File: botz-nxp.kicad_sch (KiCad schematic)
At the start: 12 parts, among them IC1 MCXA265VLH, J1 microSD, J2 JST_1mm_4, U2 MCP2561-E-MF, U3 MCP2561-E-MF

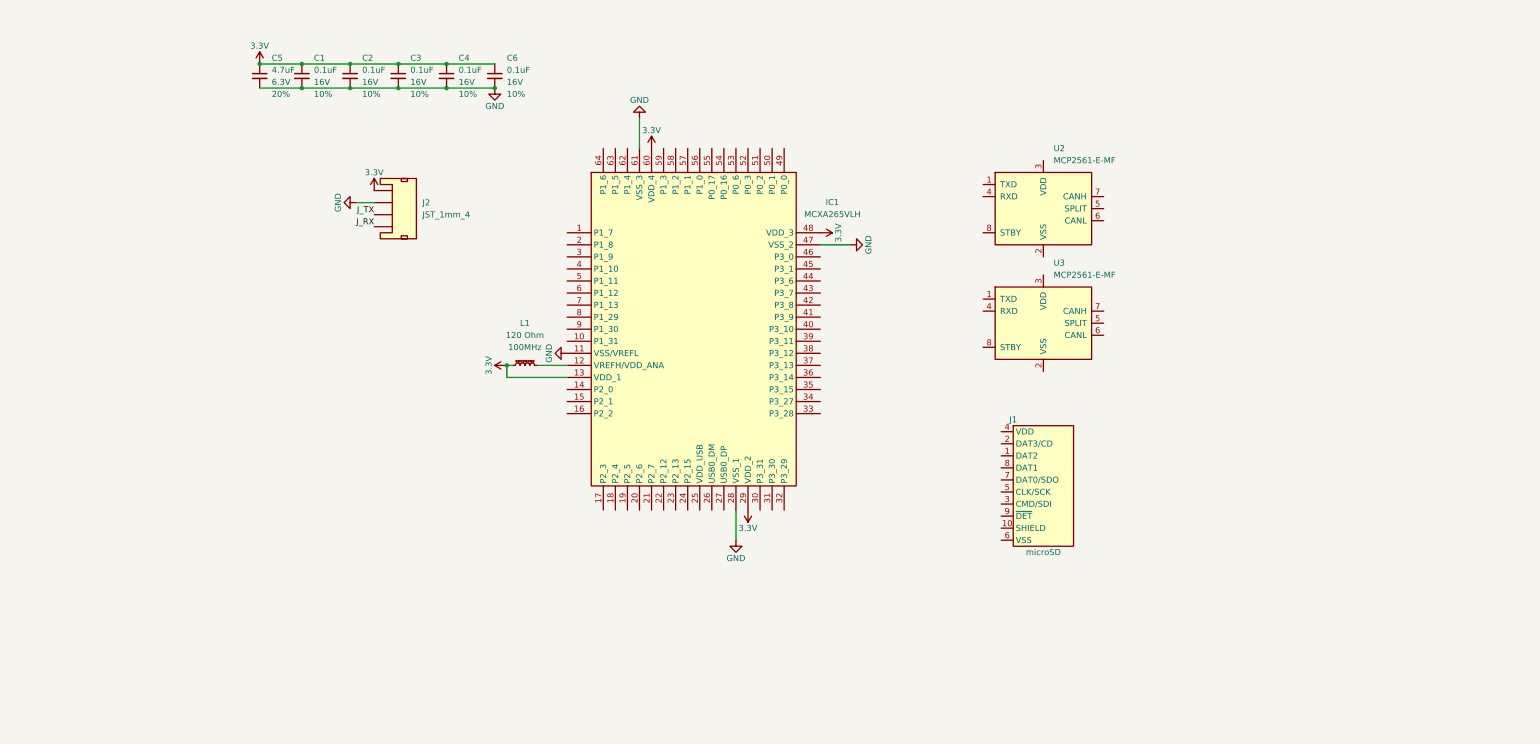
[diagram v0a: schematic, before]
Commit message: Wire CAN0/CAN1, microSD (SPI), reset, crystal, SWD header
- CAN0 on P1_2/P1_3, CAN1 on P1_1/P1_0 (ALT11), MCP2561 transceivers
- 120R termination, jumper-selectable (JP1/JP2)
- microSD on LPSPI1 (P3_8-P3_11), pull-ups, card detect on P2_2
- NRST pull-up + filter cap, crystal on P1_30/P1_31 (15pF placeholder)
- 10-pin Cortex SWD header on P0_0-P0_2
- Bulk cap swapped to 10uF 25V; VDDA filter caps after L1
- Commit lib/ and library tables so the project opens on other machines
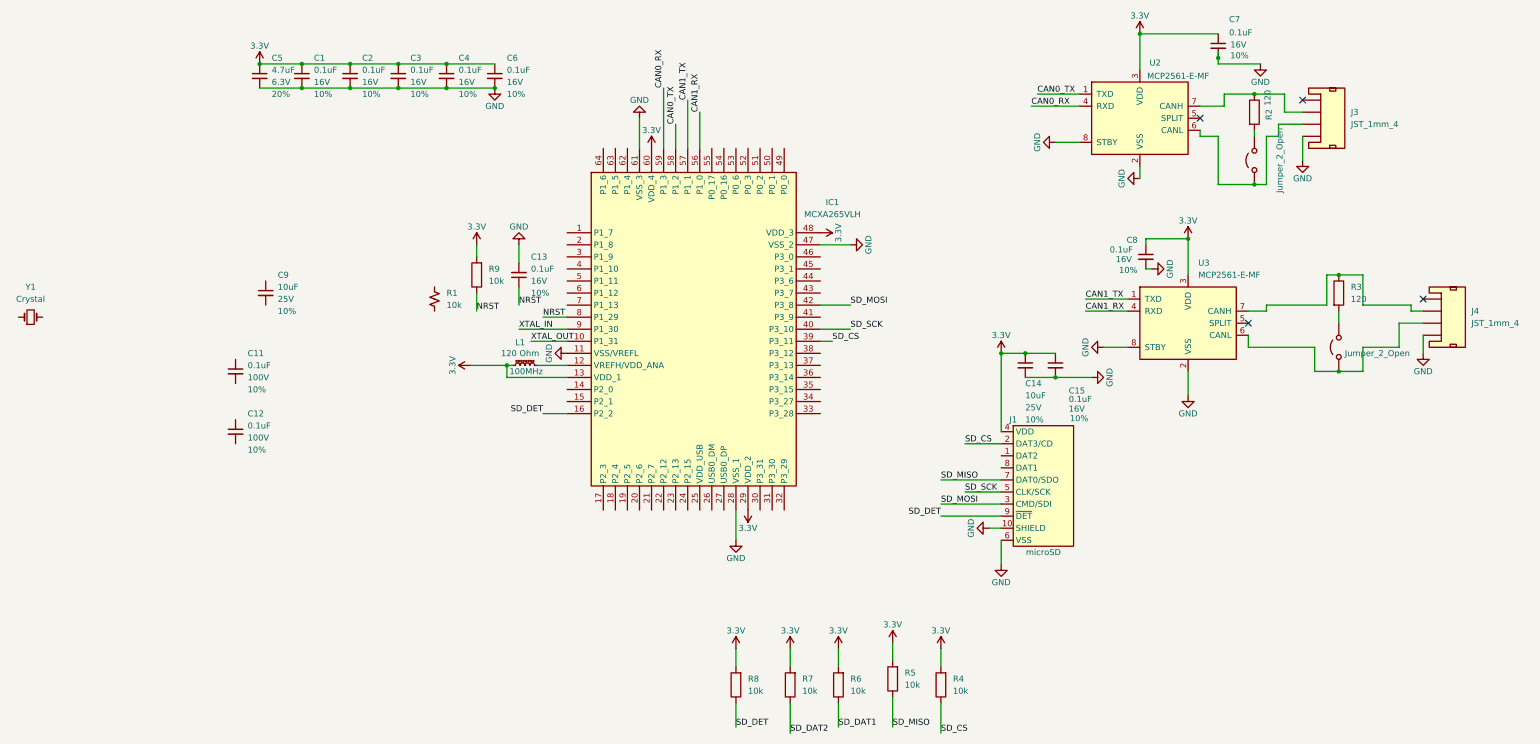
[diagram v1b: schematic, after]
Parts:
- removed J2: JST_1mm_4, PCM_SparkFun-Connector:JST_1x04_P1.0mm_Horizontal_SMD, symbol PCM_SparkFun-Connector:Conn_01x04_JST_P1.0mm_Horizontal_SMD
- added C11, C12: 0.1uF, PCM_SparkFun-Capacitor:C_0603_1608Metric, symbol PCM_SparkFun-Capacitor:0.1uF_0603_100V_10%
- added C13, C15, C7, C8: 0.1uF, PCM_SparkFun-Capacitor:C_0402_1005Metric, symbol PCM_SparkFun-Capacitor:0.1uF_0402_16V_10%
- added C14: 10uF, PCM_SparkFun-Capacitor:C_0805_2012Metric, symbol PCM_SparkFun-Capacitor:10uF_0805_25V_10%
- added C9: 10uF, PCM_SparkFun-Capacitor:C_0402_1005Metric, symbol PCM_SparkFun-Capacitor:0.1uF_0402_16V_10%
- added J3, J4: JST_1mm_4, PCM_SparkFun-Connector:JST_1x04_P1.0mm_Horizontal_SMD, symbol PCM_SparkFun-Connector:Conn_01x04_JST_P1.0mm_Horizontal_SMD
- added JP1, JP2: Jumper_2_Open, symbol Jumper:Jumper_2_Open
- added R1: 10k, PCM_SparkFun-Resistor:R_0402_1005Metric, symbol PCM_SparkFun-Resistor:10k_0402
- added R2, R3: 120, symbol Device:R
- added R4, R5, R6, R7, R8, R9: 10k, symbol Device:R
- added Y1: Crystal, PCM_SparkFun-Clock:Crystal-SMD-5x3.2mm, symbol PCM_SparkFun-Clock:Crystal
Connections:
- net 3.3V: now also J1.4 (VDD), U2.3 (VDD), U3.3 (VDD), C14.1, C15.1, C7.1, C8.1, R4.2, R5.2, R6.2, R7.2, R8.2, R9.2
- net GND: now also J1.10 (SHIELD), J1.6 (VSS), U2.2 (VSS), U2.8 (STBY), U2.9 (VSS), U3.2 (VSS), U3.8 (STBY), U3.9 (VSS), C13.2, C14.2, C15.2, C7.2, C8.2, J3.4, J4.4
- net SD_CS: now reaches J1.2 (DAT3/CD)
- net SD_CS: now also IC1.39 (P3_11), R4.1
- net SD_MOSI: now reaches J1.3 (CMD/SDI)
- net SD_MOSI: now also IC1.42 (P3_8)
- net SD_SCK: now reaches J1.5 (CLK/SCK)
- net SD_SCK: now also IC1.40 (P3_10)
- net SD_MISO: now reaches J1.7 (DAT0/SDO)
- net SD_MISO: now also R5.1
- net SD_DET: now reaches J1.9 (~{DET})
- net SD_DET: now also IC1.16 (P2_2), R8.1
- net CAN0_TX: now reaches U2.1 (TXD)
- net CAN0_TX: now also IC1.58 (P1_2)
- net CAN0_RX: now reaches U2.4 (RXD)
- net CAN0_RX: now also IC1.59 (P1_3)
- net at U2.6 (CANL): now also J3.3, JP1.1 (A)
- net at U2.7 (CANH): now also J3.2, R2.1
- net CAN1_TX: now reaches U3.1 (TXD)
- net CAN1_TX: now also IC1.57 (P1_1)
- net CAN1_RX: now reaches U3.4 (RXD)
- net CAN1_RX: now also IC1.56 (P1_0)
- net at U3.6 (CANL): now also J4.3, JP2.1 (A)
- net at U3.7 (CANH): now also J4.2, R3.1
- net XTAL_OUT: now reaches IC1.10 (P1_31)
- net NRST: now reaches IC1.8 (P1_29)
- net NRST: now also C13.1, R9.1
- net XTAL_IN: now reaches IC1.9 (P1_30)
- new net: JP2.2 (B), R3.2
- new net: JP1.2 (B), R2.2
- new net SD_DAT1: R6.1
- new net SD_DAT2: R7.1
- no-connect marks 0 -> 4
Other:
- moved on the sheet: U2, U3
